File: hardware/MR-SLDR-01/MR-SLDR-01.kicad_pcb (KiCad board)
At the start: 2 copper layers, 89.3 x 68 mm, 139 parts, among them J1 Conn_01x02_Pin, J10 Conn_01x02_Pin, J2 Conn_01x04_Pin, J3 USB_B_Micro, J4 Conn_02x05_Odd_Even, J5 Conn_01x04_Socket, J6 Conn_01x06_Pin, J7 Conn_02x04_Odd_Even, J8 Conn_01x02_Pin, J9 Conn_01x02_Pin, Q1 BC817, Q2 BC817, Q3 IRLML6402, Q4 QM6006D, Q5 QM6006D, Q6 BC817, Q7 BC817, Q8 BC817, Q9 BC817, U1 BM3451, U4 ESP32-WROOM-E, U5 CP2102N-Axx-xQFN28, U6 DRV8825, U7 93CxxC, U8 PC817, U9 PC817

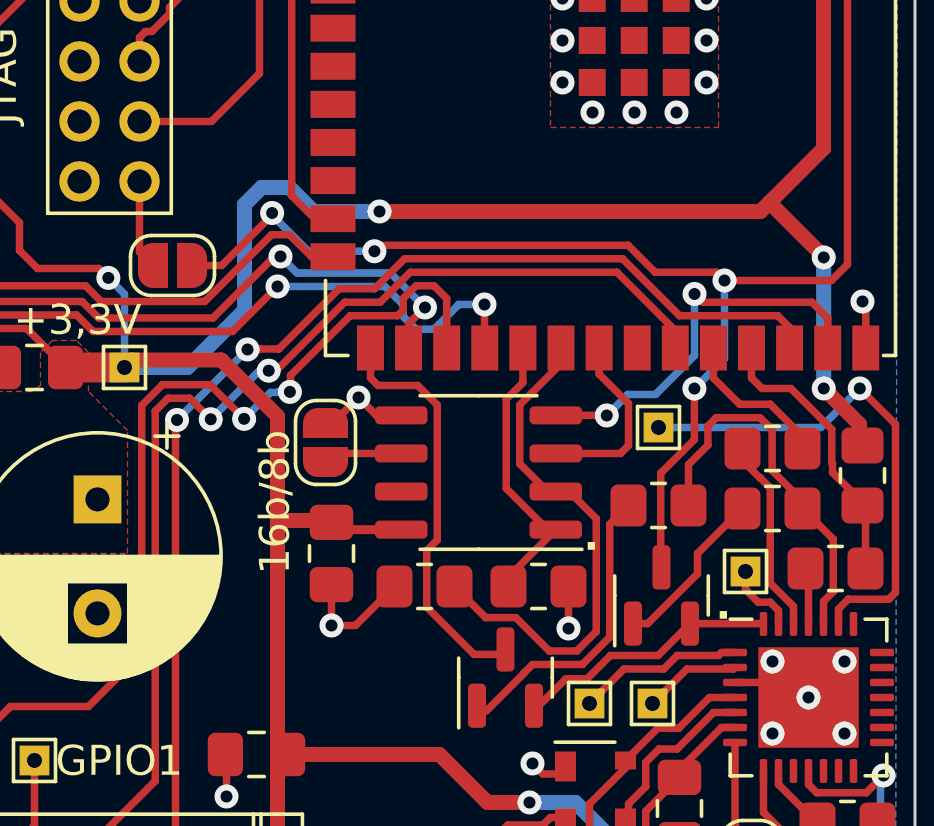
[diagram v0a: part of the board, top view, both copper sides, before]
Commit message: v0.8 MM added rangefinder; move bt handler from main.c to slider_bt.c
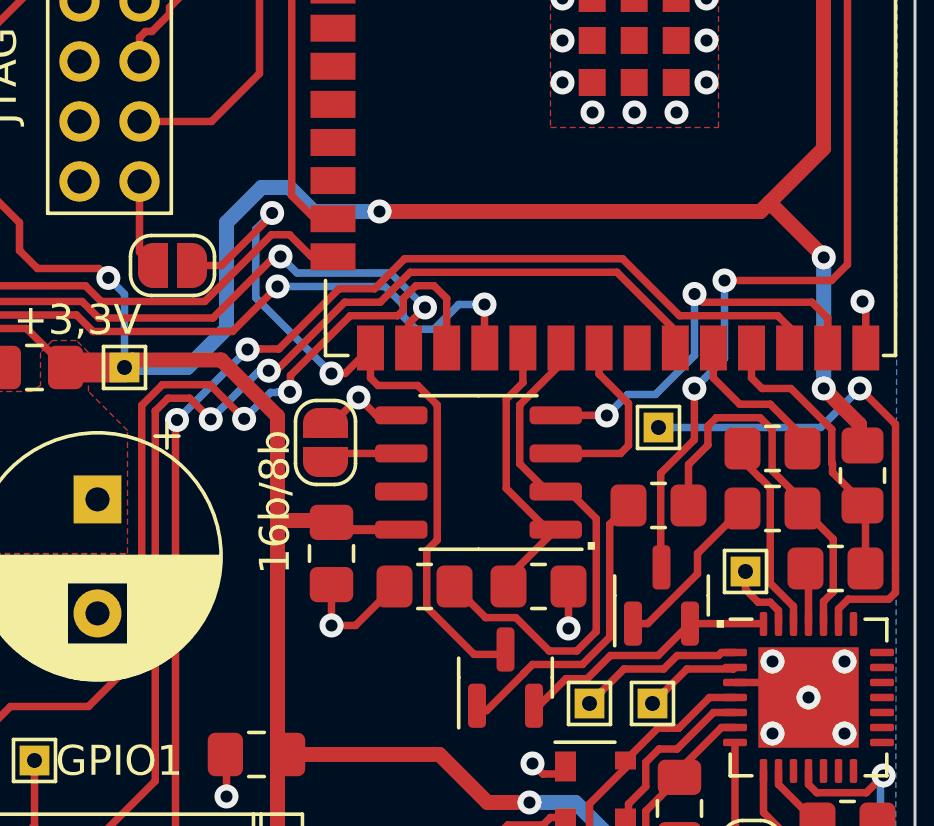
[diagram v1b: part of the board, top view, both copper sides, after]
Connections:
- JP2 pad 2: ESP32.EN -> ESP32.BOOT
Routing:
- net ESP32.EN: track 51.1 -> 31.5 mm, vias 6 -> 4
- net ESP32.BOOT: track 13.8 -> 25.5 mm, vias 0 -> 2
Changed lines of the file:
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@@
       ))
     (pad "2" smd custom (at 0.65 0) (size 1 0.5) (layers "F.Cu" "F.Mask")
-      (net 31 "ESP32.EN") (pinfunction "B") (pintype "passive") (zone_connect 2) (thermal_bridge_angle 45)
+      (net 29 "ESP32.BOOT") (pinfunction "B") (pintype "passive") (zone_connect 2) (thermal_bridge_angle 45)
       (options (clearance outline) (anchor rect))
       (primitives
@@
     (effects (font (size 1 1) (thickness 0.25) bold) (justify left bottom))
   )
-  (gr_text "." (at 179.1 125.1) (layer "F.SilkS")
+  (gr_text "." (at 179 125.4) (layer "F.SilkS")
     (effects (font (size 1 1) (thickness 0.25) bold) (justify left bottom))
   )
@@
   (via (at 176.708216 133.376027) (size 0.8) (drill 0.4) (layers "F.Cu" "B.Cu") (net 4))
   (via (at 167.9 111.4) (size 0.8) (drill 0.4) (layers "F.Cu" "B.Cu") (net 4))
+  (segment (start 163.969095 110.6005) (end 164.9005 110.6005) (width 0.5) (layer "B.Cu") (net 4))
+  (segment (start 161.5 116.6) (end 162.8 115.3) (width 0.5) (layer "B.Cu") (net 4))
   (segment (start 176.708216 133.376027) (end 174.432189 131.1) (width 0.5) (layer "B.Cu") (net 4))
+  (segment (start 162.8 115.3) (end 162.8 111.769595) (width 0.5) (layer "B.Cu") (net 4))
   (segment (start 164.9005 110.6005) (end 165.7 111.4) (width 0.5) (layer "B.Cu") (net 4))
-  (segment (start 163.969095 110.6005) (end 164.9005 110.6005) (width 0.5) (layer "B.Cu") (net 4))
   (segment (start 159.4 114.15261) (end 158.861445 113.614055) (width 0.25) (layer "B.Cu") (net 4))
-  (segment (start 161.5 116.6) (end 163.4 114.7) (width 0.5) (layer "B.Cu") (net 4))
+  (segment (start 159.4 116.6) (end 161.5 116.6) (width 0.5) (layer "B.Cu") (net 4))
   (segment (start 144.200497 108.6495) (end 144.200498 108.649499) (width 0.25) (layer "B.Cu") (net 4))
+  (segment (start 165.7 111.4) (end 167.9 111.4) (width 0.5) (layer "B.Cu") (net 4))
+  (segment (start 162.8 111.769595) (end 163.969095 110.6005) (width 0.5) (layer "B.Cu") (net 4))
   (segment (start 144.200498 108.649499) (end 144.200498 106.0005) (width 0.25) (layer "B.Cu") (net 4))
   (segment (start 182.707862 117.299502) (end 182.707862 112.932362) (width 0.5) (layer "B.Cu") (net 4))
-  (segment (start 159.4 116.6) (end 161.5 116.6) (width 0.5) (layer "B.Cu") (net 4))
   (segment (start 159.4 116.6) (end 159.4 114.15261) (width 0.25) (layer "B.Cu") (net 4))
-  (segment (start 163.4 114.7) (end 163.4 111.169595) (width 0.5) (layer "B.Cu") (net 4))
-  (segment (start 163.4 111.169595) (end 163.969095 110.6005) (width 0.5) (layer "B.Cu") (net 4))
-  (segment (start 165.7 111.4) (end 167.9 111.4) (width 0.5) (layer "B.Cu") (net 4))
   (segment (start 174.432189 131.1) (end 172.9 131.1) (width 0.5) (layer "B.Cu") (net 4))
   (segment (start 105.8 125.936827) (end 106.15 126.286827) (width 0.25) (layer "F.Cu") (net 5))
@@
   (segment (start 172.1 126.1625) (end 171.049327 126.1625) (width 0.25) (layer "F.Cu") (net 29))
   (segment (start 169.825 117.848249) (end 169.176751 117.2) (width 0.25) (layer "F.Cu") (net 29))
+  (segment (start 166.3 116.8) (end 166.75 116.8) (width 0.25) (layer "F.Cu") (net 29))
   (segment (start 169.475 122.701751) (end 169.825 122.351751) (width 0.25) (layer "F.Cu") (net 29))
   (segment (start 169.825 122.351751) (end 169.825 117.848249) (width 0.25) (layer "F.Cu") (net 29))
@@
   (segment (start 169.176751 117.2) (end 167.85 117.2) (width 0.25) (layer "F.Cu") (net 29))
   (segment (start 169.475 124.588173) (end 169.475 122.701751) (width 0.25) (layer "F.Cu") (net 29))
+  (segment (start 164.321177 111.4505) (end 164.321177 111.517122) (width 0.25) (layer "F.Cu") (net 29))
+  (segment (start 166.75 116.8) (end 167.6 115.95) (width 0.25) (layer "F.Cu") (net 29))
+  (segment (start 162.638299 113.2) (end 161.65 113.2) (width 0.25) (layer "F.Cu") (net 29))
+  (segment (start 164.321177 111.517122) (end 162.638299 113.2) (width 0.25) (layer "F.Cu") (net 29))
   (segment (start 167.6 116.95) (end 167.6 115.95) (width 0.25) (layer "F.Cu") (net 29))
+  (via (at 166.3 116.8) (size 0.8) (drill 0.4) (layers "F.Cu" "B.Cu") (net 29))
+  (via (at 164.321177 111.4505) (size 0.8) (drill 0.4) (layers "F.Cu" "B.Cu") (net 29))
+  (segment (start 163.775 114.275) (end 166.3 116.8) (width 0.25) (layer "B.Cu") (net 29))
+  (segment (start 163.775 111.996677) (end 163.775 114.275) (width 0.25) (layer "B.Cu") (net 29))
+  (segment (start 163.775 111.996677) (end 164.321177 111.4505) (width 0.25) (layer "B.Cu") (net 29))
   (segment (start 166.15 96.1375) (end 166.640749 96.1375) (width 0.25) (layer "F.Cu") (net 30))
   (segment (start 168.478249 94.3) (end 169.9 94.3) (width 0.25) (layer "F.Cu") (net 30))
   (segment (start 166.640749 96.1375) (end 168.478249 94.3) (width 0.25) (layer "F.Cu") (net 30))
   (segment (start 183.5 100.9645) (end 183.5 113.164823) (width 0.25) (layer "F.Cu") (net 31))
-  (segment (start 167.730694 112.7255) (end 167.930696 112.525498) (width 0.25) (layer "F.Cu") (net 31))
-  (segment (start 167.930696 112.525498) (end 176.18829 112.525498) (width 0.25) (layer "F.Cu") (net 31))
   (segment (start 177.275 120.125) (end 177.275 123.2375) (width 0.25) (layer "F.Cu") (net 31))
   (segment (start 178.396672 117.301849) (end 178.396672 119.003328) (width 0.25) (layer "F.Cu") (net 31))
   (segment (start 181.57 100.869999) (end 181.57 98.45) (width 0.25) (layer "F.Cu") (net 31))
   (segment (start 183.5 113.164823) (end 182.964323 113.7005) (width 0.25) (layer "F.Cu") (net 31))
-  (segment (start 164.321177 111.4505) (end 164.321177 111.517122) (width 0.25) (layer "F.Cu") (net 31))
-  (segment (start 179.125 113.4255) (end 179.4 113.7005) (width 0.25) (layer "F.Cu") (net 31))
   (segment (start 177.275 123.2375) (end 177.3 123.2625) (width 0.25) (layer "F.Cu") (net 31))
-  (segment (start 176.18829 112.525498) (end 177.088292 113.4255) (width 0.25) (layer "F.Cu") (net 31))
-  (segment (start 162.638299 113.2) (end 161.65 113.2) (width 0.25) (layer "F.Cu") (net 31))
   (segment (start 181.6 100.899999) (end 181.57 100.869999) (width 0.25) (layer "F.Cu") (net 31))
-  (segment (start 164.321177 111.517122) (end 162.638299 113.2) (width 0.25) (layer "F.Cu") (net 31))
-  (segment (start 177.088292 113.4255) (end 179.125 113.4255) (width 0.25) (layer "F.Cu") (net 31))
   (segment (start 183.5645 100.9) (end 183.5 100.9645) (width 0.25) (layer "F.Cu") (net 31))
   (segment (start 178.396672 119.003328) (end 177.275 120.125) (width 0.25) (layer "F.Cu") (net 31))
   (segment (start 182.964323 113.7005) (end 179.4 113.7005) (width 0.25) (layer "F.Cu") (net 31))
-  (via (at 164.321177 111.4505) (size 0.8) (drill 0.4) (layers "F.Cu" "B.Cu") (net 31))
   (via (at 178.396672 117.301849) (size 0.8) (drill 0.4) (layers "F.Cu" "B.Cu") (net 31))
   (via (at 179.4 113.7005) (size 0.8) (drill 0.4) (layers "F.Cu" "B.Cu") (net 31))
   (via (at 181.6 100.899999) (size 0.8) (drill 0.4) (layers "F.Cu" "B.Cu") (net 31))
-  (via (at 167.730694 112.7255) (size 0.8) (drill 0.4) (layers "F.Cu" "B.Cu") (net 31))
   (via (at 183.5645 100.9) (size 0.8) (drill 0.4) (layers "F.Cu" "B.Cu") (net 31))
-  (segment (start 165.5255 112.7255) (end 167.730694 112.7255) (width 0.25) (layer "B.Cu") (net 31))
   (segment (start 181.6 100.899999) (end 181.600001 100.9) (width 0.25) (layer "B.Cu") (net 31))
   (segment (start 179.4 113.7005) (end 179.4 116.298521) (width 0.25) (layer "B.Cu") (net 31))
-  (segment (start 164.321177 111.521177) (end 165.5255 112.7255) (width 0.25) (layer "B.Cu") (net 31))
   (segment (start 179.4 116.298521) (end 178.396672 117.301849) (width 0.25) (layer "B.Cu") (net 31))
-  (segment (start 164.321177 111.4505) (end 164.321177 111.521177) (width 0.25) (layer "B.Cu") (net 31))
   (segment (start 181.600001 100.9) (end 183.5645 100.9) (width 0.25) (layer "B.Cu") (net 31))
   (segment (start 108.1 117.1) (end 108.1 116.7) (width 0.25) (layer "F.Cu") (net 32))
